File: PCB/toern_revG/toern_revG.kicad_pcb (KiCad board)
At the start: 4 copper layers, 160 x 71 mm, 105 parts, among them IC1 BQ24075TRGTR, J1 AudioJack3_Switch, J10 Conn_01x02, J11 Conn_01x05, J11.5 Conn_01x05, J12 Conn_01x05, J13 Conn_01x05, J14 Conn_01x05, J15 Conn_01x05, J16 Conn_01x02, J17 AudioJack3_Ground, J18 Conn_01x05_Socket, J19 Conn_01x05_Socket, J2 Conn_01x05_Socket, J20 Conn_01x05_Socket, J21 Conn_01x05_Socket, J22 Conn_01x05_Socket, J23 Conn_01x05_Socket, J24 Conn_01x05_Socket, J3 AudioJack3_Ground, J4 USB_C_Receptacle_USB2.0, J5 AudioJack3_Switch, J6 AudioJack3_Switch, J7 AudioJack3_Switch, J8 Micro_SD_Card, J9 Conn_01x03, U1 SPX3819M5-L-3-3, U13 PAM8403D, U2 SPX3819M5-L-1-8, U3 SGTL5000XNBA3, U4 TLP2361V4_E, U5 74LVC2G14, U6 Teensy4.1, U7 SPX3819M5-L-3-3

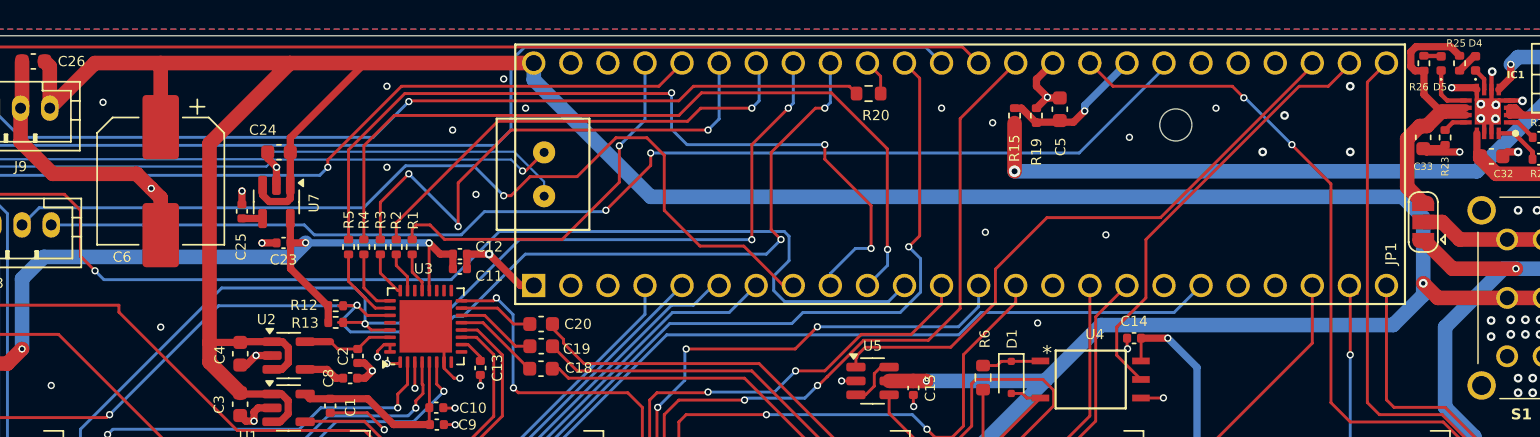
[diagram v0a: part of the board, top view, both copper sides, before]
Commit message: small fixes in code, additional TPS22918DBVR for PCB (leds)
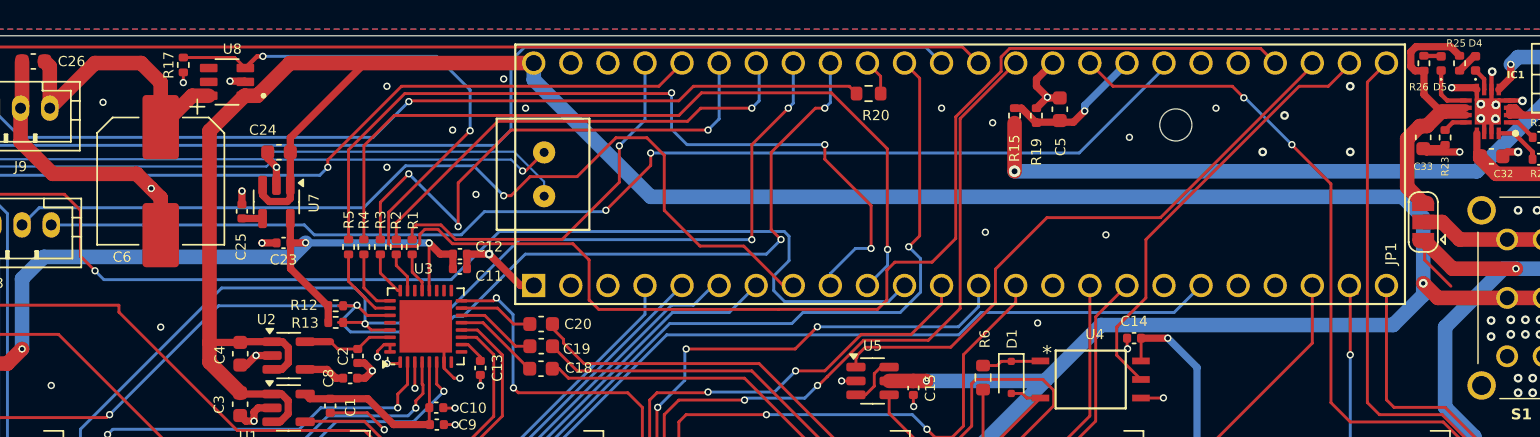
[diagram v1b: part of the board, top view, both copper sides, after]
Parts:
- added R17: 10k, Resistor_SMD:R_0402_1005Metric, F.Cu at (91.5, 27.0)
- added U8: TPS22918DBVR, TPS22918DBVR:SOT95P280X145-6N, F.Cu at (94.5, 28.2)
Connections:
- C26 pad 1: +5V -> Net-(J9-Pin_3)
- C6 pad 1: +5V -> Net-(J9-Pin_3)
- J9 pad 3: +5V -> Net-(J9-Pin_3)
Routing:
- net 36_CS: track 0.00 -> 114.8 mm, vias 0 -> 2
- net +5V: track 488.2 -> 458.3 mm
- net Net-(J9-Pin_3): track 0.00 -> 20.0 mm
- net VBUS: track 303.4 -> 307.3 mm
- net GND: track 134.5 -> 136.3 mm, vias 154 -> 156

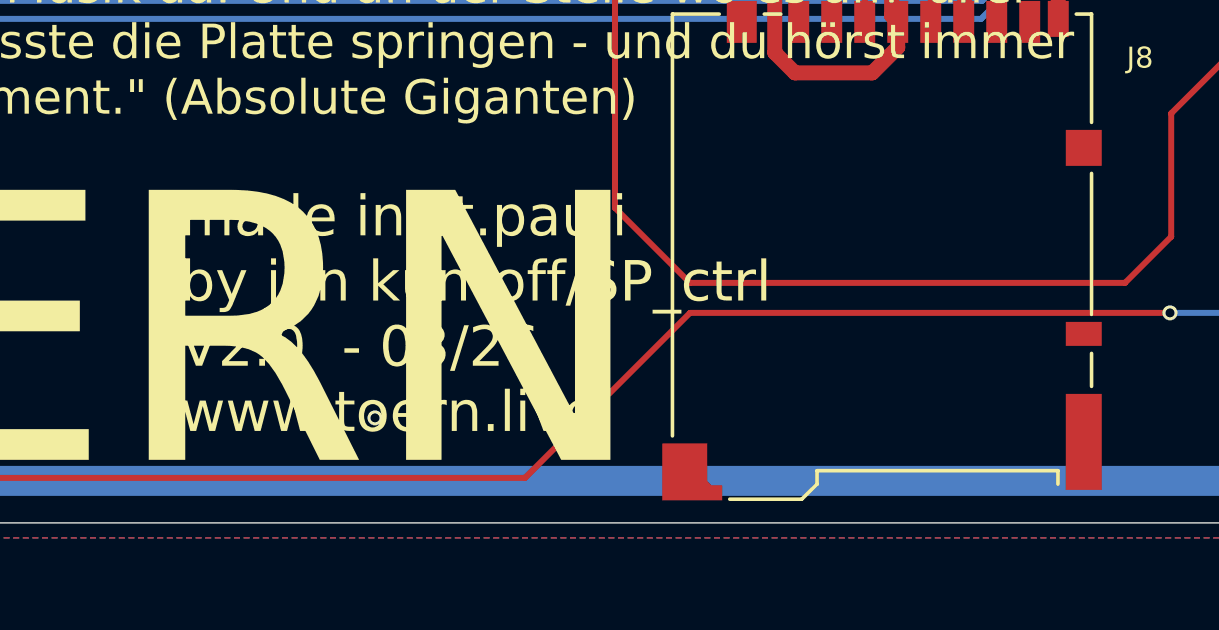
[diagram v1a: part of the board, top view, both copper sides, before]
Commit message: fixed audio/pack loading and handling, also added eyes screensaver
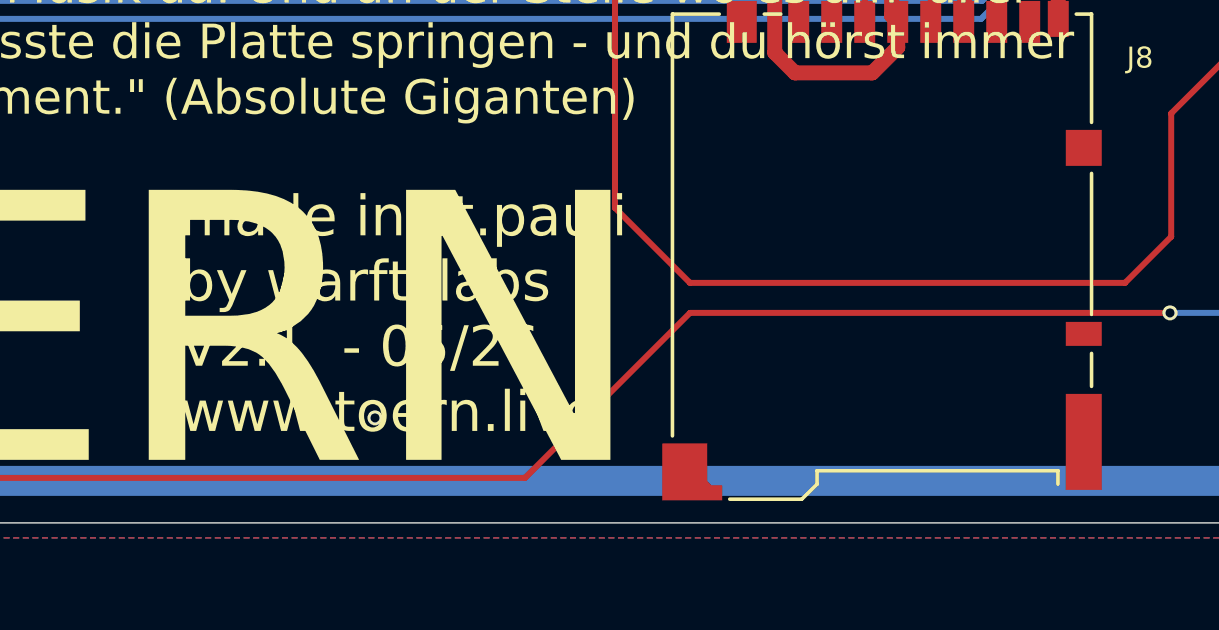
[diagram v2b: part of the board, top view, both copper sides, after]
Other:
- board text added: "made in st.pauli by warft_labs V2.1 - 05/26 www.toern.live"
- board text removed: "made in st.pauli by jan kuntoff/SP_ctrl V2.0 - 03/26 www.toern.live"

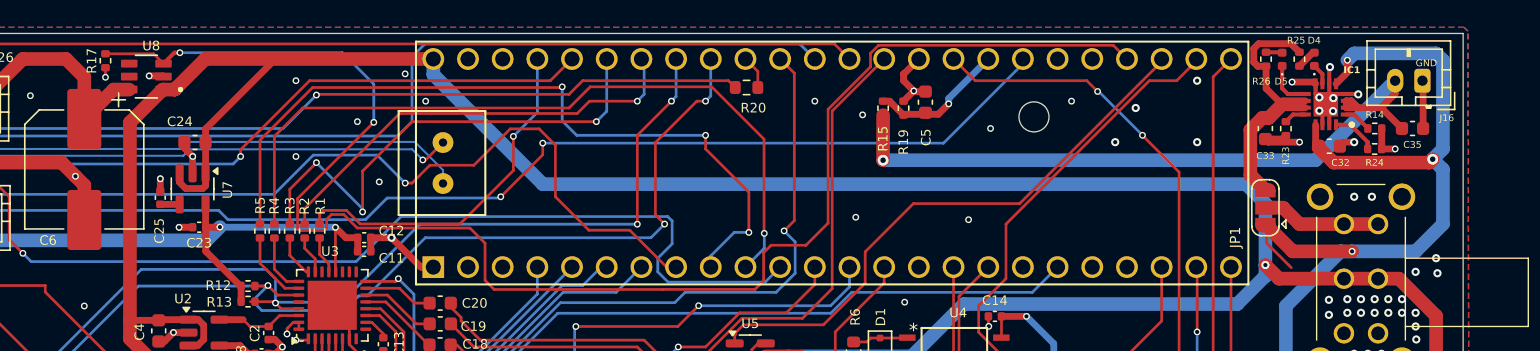
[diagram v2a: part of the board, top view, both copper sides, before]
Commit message: fixed PCB: right resistors for TS + componentsize - final
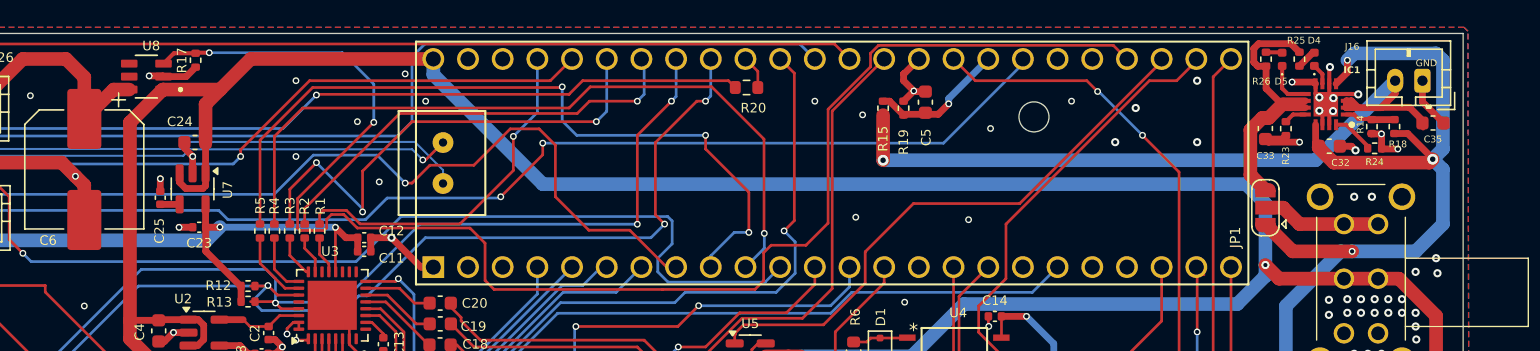
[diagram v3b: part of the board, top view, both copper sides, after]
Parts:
- added R18: 47k, Resistor_SMD:R_0402_1005Metric, F.Cu at (185.9, 31.9)
- moved R17 6.60 mm to (98.2, 27.0)
- moved C35 1.55 mm to (188.8, 31.6)
- moved R14 0.25 mm to (184.3, 31.9), turned to -90 degrees
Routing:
- net 36_CS: track 114.8 -> 110.1 mm
- net +5V: track 458.3 -> 454.2 mm
- net GND: track 136.3 -> 139.2 mm
- net Net-(IC1-TS): track 2.01 -> 3.68 mm
- net VBAT: track 51.9 -> 53.4 mm
- net Net-(IC1-ISET): track 3.85 -> 3.12 mm
